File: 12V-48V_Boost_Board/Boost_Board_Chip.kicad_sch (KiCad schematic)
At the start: 23 parts, among them Q1 FDWS86068-F085

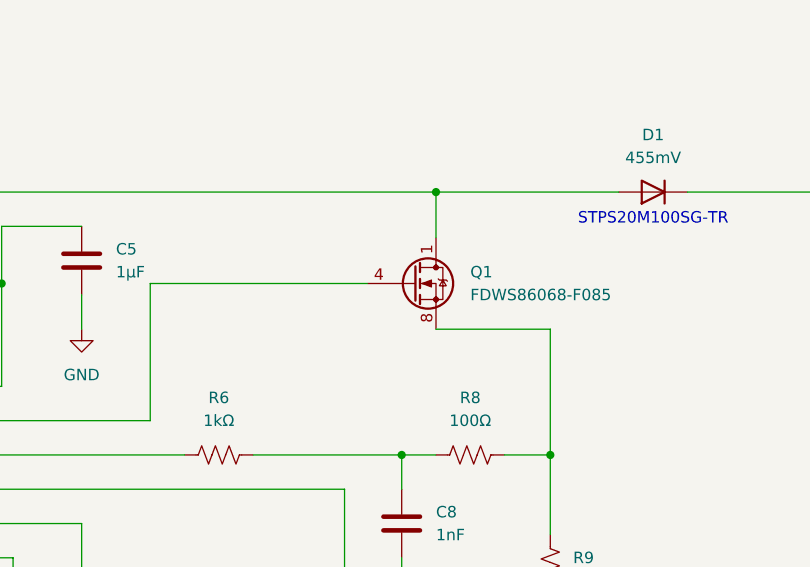
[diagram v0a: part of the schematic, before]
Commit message: Updated as review, let me know if I should just redo the layout completely cause its still a bit scuffed imo
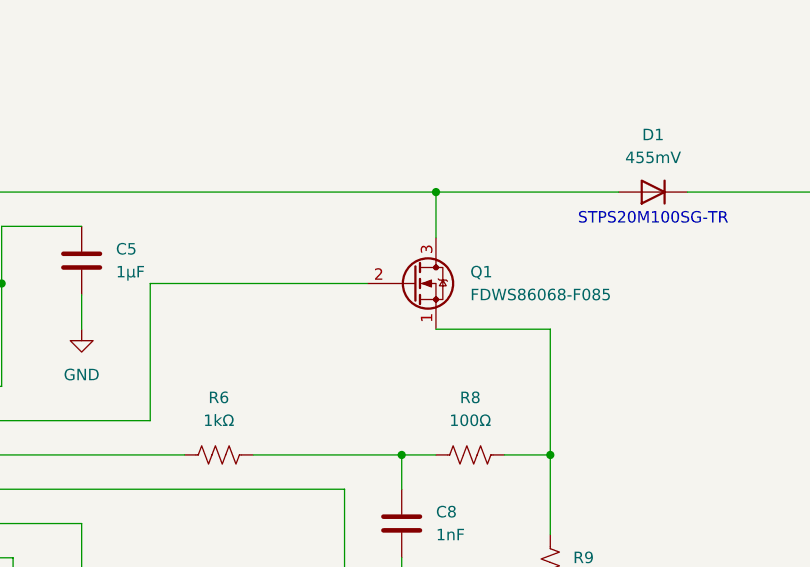
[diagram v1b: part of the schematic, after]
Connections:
- net at U1.4 (GATE): now also Q1.2 (G); no longer Q1.4 (G)
- net at D1.1 (A), L1.2: now also Q1.3 (D); no longer Q1.1 (D)
- net at R8.2, R9.1: now also Q1.1 (S); no longer Q1.8 (S)
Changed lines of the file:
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@@
 		(pin "1"
 		)
-		(pin "4"
+		(pin "2"
 		)
-		(pin "8"
+		(pin "3"
 		)
 		(instances

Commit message: Changed layout to make it more compact, changed output and input cap sizes
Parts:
- C1, C2: footprint Capacitor_SMD:C_0805_2012Metric_Pad1.18x1.45mm_HandSolder -> 12/48 boost:GRM31CR71H475KA12L
- C10, C11, C9: footprint Capacitor_SMD:C_0805_2012Metric_Pad1.18x1.45mm_HandSolder -> 12/48 boost:CAPC6050X550N
- C12: footprint Capacitor_SMD:C_0805_2012Metric_Pad1.18x1.45mm_HandSolder -> 12/48 boost:CAPC3216X180N
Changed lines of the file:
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@@
 			)
 		)
-		(property "Footprint" "Capacitor_SMD:C_0805_2012Metric_Pad1.18x1.45mm_HandSolder"
+		(property "Footprint" "12/48 boost:CAPC6050X550N"
 			(at 240.9952 97.79 0)
 			(effects
@@
 			)
 		)
-		(property "Datasheet" "~"
+		(property "Datasheet" "https://datasheets.kyocera-avx.com/X7RDielectric.pdf"
 			(at 240.03 93.98 0)
 			(effects
@@
 			)
 		)
-		(property "Description" "Unpolarized capacitor"
+		(property "Description" "08053C104KAT2A"
 			(at 240.03 93.98 0)
 			(effects
@@
 			)
 		)
-		(property "Footprint" "Capacitor_SMD:C_0805_2012Metric_Pad1.18x1.45mm_HandSolder"
+		(property "Footprint" "12/48 boost:CAPC6050X550N"
 			(at 229.5652 105.41 0)
 			(effects
@@
 			)
 		)
-		(property "Datasheet" "~"
+		(property "Datasheet" "https://datasheets.kyocera-avx.com/X7RDielectric.pdf"
 			(at 228.6 101.6 0)
 			(effects
@@
 			)
 		)
-		(property "Description" "Unpolarized capacitor"
+		(property "Description" "08053C104KAT2A"
 			(at 228.6 101.6 0)
 			(effects
@@
 			)
 		)
-		(property "Footprint" "Capacitor_SMD:C_0805_2012Metric_Pad1.18x1.45mm_HandSolder"
+		(property "Footprint" "12/48 boost:CAPC6050X550N"
 			(at 251.1552 109.22 0)
 			(effects
@@
 			)
 		)
-		(property "Datasheet" "~"
+		(property "Datasheet" "https://datasheets.kyocera-avx.com/X7RDielectric.pdf"
 			(at 250.19 105.41 0)
 			(effects
@@
 			)
 		)
-		(property "Description" "Unpolarized capacitor"
+		(property "Description" "08053C104KAT2A"
 			(at 250.19 105.41 0)
 			(effects
@@
 			)
 		)
-		(property "Footprint" "Capacitor_SMD:C_0805_2012Metric_Pad1.18x1.45mm_HandSolder"
+		(property "Footprint" "12/48 boost:GRM31CR71H475KA12L"
 			(at 54.3052 102.87 0)
 			(effects
@@
 			)
 		)
-		(property "Footprint" "Capacitor_SMD:C_0805_2012Metric_Pad1.18x1.45mm_HandSolder"
+		(property "Footprint" "12/48 boost:GRM31CR71H475KA12L"
 			(at 36.5252 102.87 0)
 			(effects
@@
 			)
 		)
-		(property "Footprint" "Capacitor_SMD:C_0805_2012Metric_Pad1.18x1.45mm_HandSolder"
+		(property "Footprint" "12/48 boost:CAPC3216X180N"
 			(at 261.3152 127 0)
 			(effects
@@
 			)
 		)
-		(property "Datasheet" "~"
+		(property "Datasheet" "https://product.tdk.com/en/system/files/dam/doc/product/capacitor/ceramic/mlcc/catalog/mlcc_commercial_midvoltage_en.pdf"
 			(at 260.35 123.19 0)
 			(effects

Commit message: Made the two resistors bigger, will implement other changes after some discussion
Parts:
- R9: footprint Resistor_SMD:R_0805_2012Metric_Pad1.20x1.40mm_HandSolder -> 12/48 boost:RES_WSL25124L000FEB
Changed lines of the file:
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@@
 			)
 		)
-		(property "Footprint" "Resistor_SMD:R_0805_2012Metric_Pad1.20x1.40mm_HandSolder"
+		(property "Footprint" "12/48 boost:RES_WSL25124L000FEB"
 			(at 190.246 103.124 90)
 			(effects
@@
 			)
 		)
-		(property "Datasheet" "~"
+		(property "Datasheet" "WSL25124L000FEB"
 			(at 189.23 102.87 0)
 			(effects

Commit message: Changed 63nF cap footprint
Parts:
- C4: footprint Capacitor_SMD:C_0805_2012Metric_Pad1.18x1.45mm_HandSolder -> Capacitor_SMD:C_1206_3216Metric_Pad1.33x1.80mm_HandSolder
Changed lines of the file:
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@@
 			)
 		)
-		(property "Description" "08053C104KAT2A"
+		(property "Description" "CKG57NX7R2A106M500JH"
 			(at 240.03 93.98 0)
 			(effects
@@
 			)
 		)
-		(property "Footprint" "Capacitor_SMD:C_0805_2012Metric_Pad1.18x1.45mm_HandSolder"
+		(property "Footprint" "Capacitor_SMD:C_1206_3216Metric_Pad1.33x1.80mm_HandSolder"
 			(at 82.2452 115.57 0)
 			(effects
@@
 			)
 		)
-		(property "Description" "08053C104KAT2A"
+		(property "Description" "CKG57NX7R2A106M500JH"
 			(at 228.6 101.6 0)
 			(effects
@@
 			)
 		)
-		(property "Description" "08053C104KAT2A"
+		(property "Description" "CKG57NX7R2A106M500JH"
 			(at 250.19 105.41 0)
 			(effects
@@
 			)
 		)
-		(property "Description" "Unpolarized capacitor"
+		(property "Description" "C3216X7R2A105M160AA"
 			(at 260.35 123.19 0)
 			(effects
